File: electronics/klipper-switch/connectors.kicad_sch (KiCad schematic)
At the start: 0 parts

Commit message: schematic naming and pico symbol update
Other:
- title: (none) -> klipper-switch, connectors
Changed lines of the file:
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@@
 	(generator_version "8.0")
 	(paper "A4")
+	(title_block
+		(title "klipper-switch, connectors")
+	)
 )

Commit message: LEDs & Molex CONNs
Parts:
- added D1, D2, D3, D4: 151031SS06000, LED_THT:LED_D3.0mm, symbol klipper-switch:151031SS06000
- added D5, D6, D7: MM3Z18VT1G, Diode_SMD:D_SOD-323_HandSoldering, symbol klipper-switch:MM3Z18VT1G
- added J1, J10, J11, J12, J13, J3, J4, J5, J6, J7, J8, J9: 430450400, KiCAD-RevB-footprint-library:0430450400, symbol klipper-switch:430450400
- added Q1, Q2, Q3: RK7002BMT116, klipper-switch:RK7002BMT116, symbol klipper-switch:RK7002BMT116
- added R1, R2, R3, R4: 100R, Resistor_SMD:R_1206_3216Metric, symbol klipper-switch:RC1206FR-7W100RL
- added R5, R6, R7: 100K, Resistor_SMD:R_1206_3216Metric, symbol klipper-switch:RC1206FR-07100KL
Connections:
- new net: D3.1 (K), Q2.3 (D)
- new net: D3.2 (A), R3.2
- new net: D1.2 (A), R1.2
- new net: D5.1 (K), Q1.2 (G), R5.2
- new net: D4.1 (K), Q3.3 (D)
- new net: D4.2 (A), R4.2
- new net: D2.1 (K), Q1.3 (D)
- new net: D2.2 (A), R2.2
- new net: D7.1 (K), Q3.2 (G), R7.2
- new net: D6.1 (K), Q2.2 (G), R6.2
- new net +12V: J3.2, J3.4, R5.1
- new net +24V: J4.2, J4.4, R6.1
- new net +48V: J5.2, J5.4, R7.1
- new net +5V: J1.2, J1.4, R1.1, R2.1, R3.1, R4.1
- new net GND: D1.1 (K), D5.2 (A), D6.2 (A), D7.2 (A), J1.1, J1.3, J3.1, J3.3, J4.1, J4.3, J5.1, J5.3, Q1.1 (S), Q2.1 (S), Q3.1 (S)
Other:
- note added: "POWER INDICATION LEDs"
- note added: "POWER INPUT CONNECTORs"
- note added: "POWER OUTPIT CONNECTORs"

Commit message: library modified
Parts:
- removed R1, R2, R3, R4: 100R, Resistor_SMD:R_1206_3216Metric, symbol klipper-switch:RC1206FR-7W100RL
- added R1, R2, R3, R4: 100R, Resistor_SMD:R_1206_3216Metric, symbol klipper-switch:RC1206FR-7W100RL_1
- D3: Role LED_12V -> LED_24V
- D4: Role LED_12V -> LED_48V
- J1: Role 05VIN -> 12VIN
- J10, J6: Role 05VIN -> ROLE
- J11, J7: Role 12VIN -> ROLE
- J12, J8: Role 24VIN -> ROLE
- J13, J9: Role 48VIN -> ROLE
- J3: Role 12VIN -> 05VIN
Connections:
- net +12V: now also J1.2, J1.4, R5.2; no longer J3.2, J3.4, R5.1
- net +24V: now also R6.2; no longer R6.1
- net +48V: now also R7.2; no longer R7.1
- net +5V: now also J3.2, J3.4, R1.1, R2.1, R3.1, R4.1; no longer J1.2, J1.4
- net at D3.1 (K): now also R3.2; no longer Q2.3 (D)
- net at D3.2 (A): now also Q2.3 (D)
- net at D1.2 (A): now also R1.2
- net at D5.1 (K), Q1.2 (G): now also R5.1; no longer R5.2
- net at D4.1 (K): now also R4.2; no longer Q3.3 (D)
- net at D4.2 (A): now also Q3.3 (D)
- net at D2.1 (K): now also R2.2; no longer Q1.3 (D)
- net at D2.2 (A): now also Q1.3 (D)
- net at D7.1 (K), Q3.2 (G): now also R7.1; no longer R7.2
- net at D6.1 (K), Q2.2 (G): now also R6.1; no longer R6.2

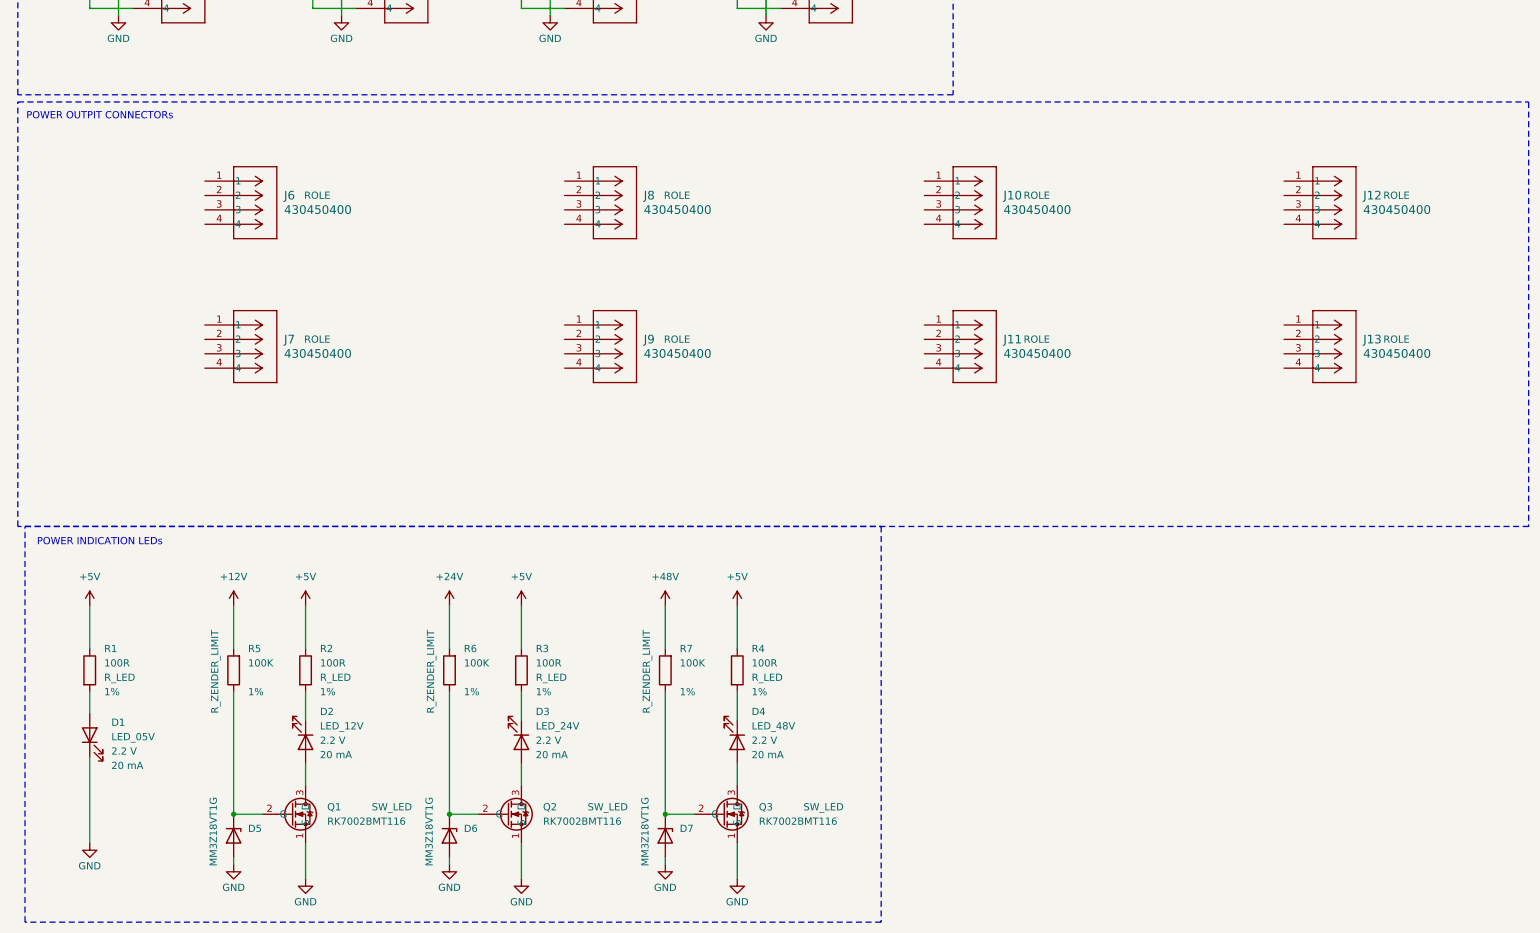
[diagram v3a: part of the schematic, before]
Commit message: output conn adjusted
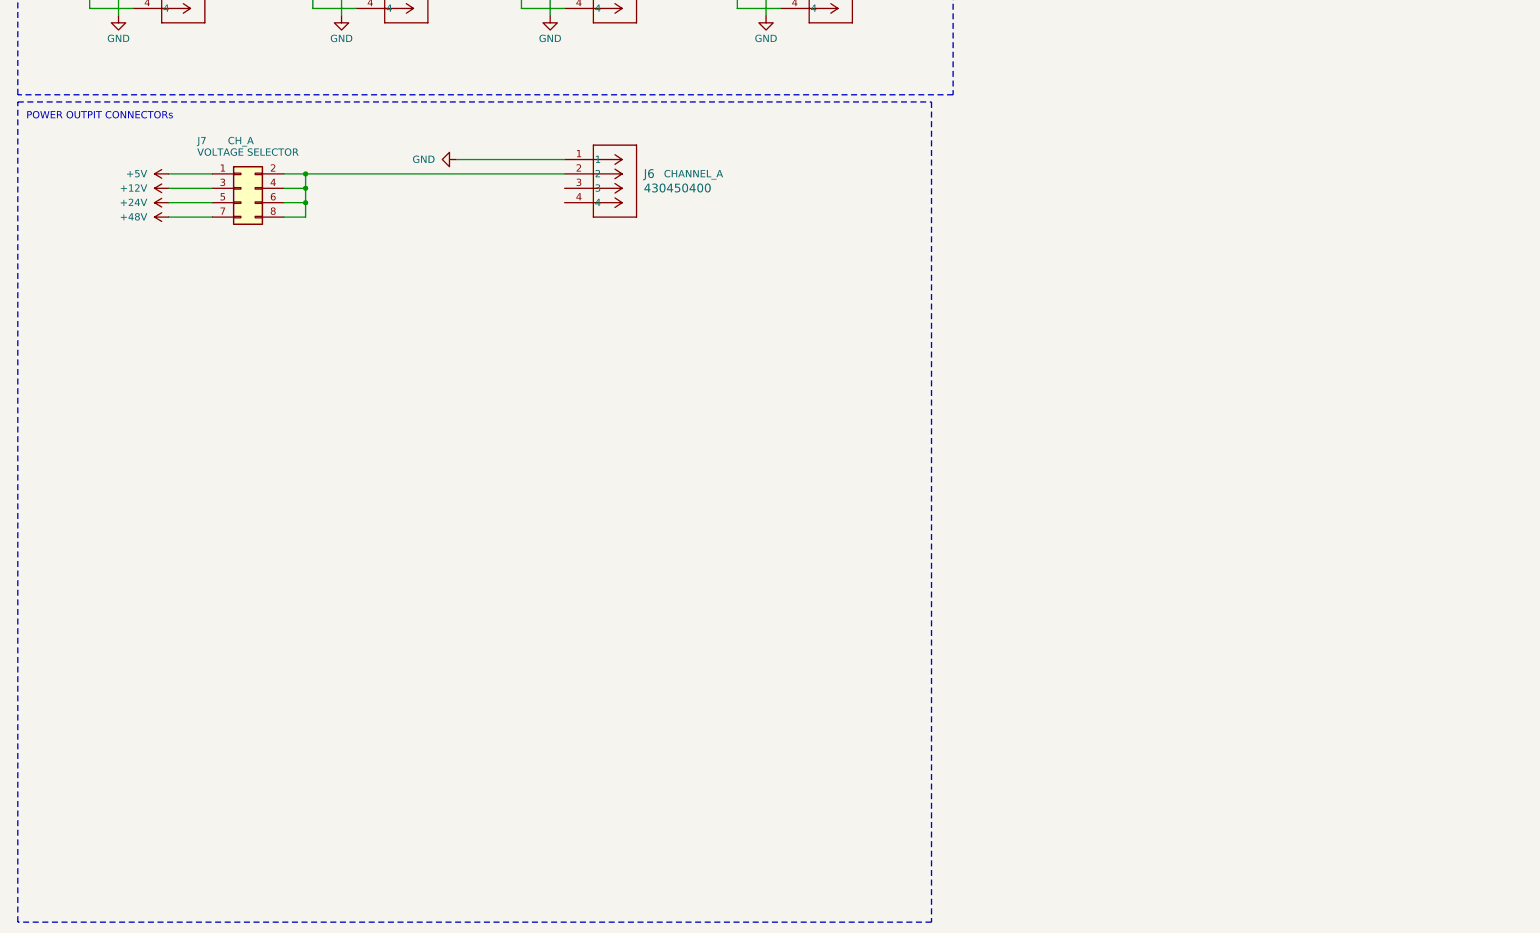
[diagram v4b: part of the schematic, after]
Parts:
- removed D1, D2, D3, D4: 151031SS06000, LED_THT:LED_D3.0mm, symbol klipper-switch:151031SS06000
- removed D5, D6, D7: MM3Z18VT1G, Diode_SMD:D_SOD-323_HandSoldering, symbol klipper-switch:MM3Z18VT1G
- removed J10, J11, J12, J13, J7, J8, J9: 430450400, KiCAD-RevB-footprint-library:0430450400, symbol klipper-switch:430450400
- removed Q1, Q2, Q3: RK7002BMT116, klipper-switch:RK7002BMT116, symbol klipper-switch:RK7002BMT116
- removed R1, R2, R3, R4: 100R, Resistor_SMD:R_1206_3216Metric, symbol klipper-switch:RC1206FR-7W100RL_1
- removed R5, R6, R7: 100K, Resistor_SMD:R_1206_3216Metric, symbol klipper-switch:RC1206FR-07100KL
- added J7: VOLTAGE SELECTOR, Connector_PinHeader_2.54mm:PinHeader_2x04_P2.54mm_Vertical, symbol Connector_Generic:Conn_02x04_Odd_Even
- J6: Role ROLE -> CHANNEL_A
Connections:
- net +12V: now also J7.3 (Pin_3)
- net +24V: now also J7.5 (Pin_5)
- net +48V: now also J7.7 (Pin_7)
- net +5V: now also J7.1 (Pin_1)
- net GND: now also J6.1
- net at J6.2: now also J7.2 (Pin_2), J7.4 (Pin_4), J7.6 (Pin_6), J7.8 (Pin_8)
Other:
- note removed: "POWER INDICATION LEDs"
- moved on the sheet: J6

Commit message: high-side switches added
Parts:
- added J10, J11, J14, J15, J18, J19, J8: VOLTAGE SELECTOR, Connector_PinHeader_2.54mm:PinHeader_2x04_P2.54mm_Vertical, symbol Connector_Generic:Conn_02x04_Odd_Even
- added J12, J13, J16, J17, J20, J21, J9: 430450400, KiCAD-RevB-footprint-library:0430450400, symbol klipper-switch:430450400
- added R10, R12, R13, R16, R17, R20, R21, R9: 5K, Resistor_SMD:R_1206_3216Metric, symbol klipper-switch:RC1206FR-7W100RL_1
- added R11, R14, R15, R18, R19, R22, R23, R8: 1K, Resistor_SMD:R_1206_3216Metric, symbol klipper-switch:RC1206FR-7W100RL_1
- added U2, U3, U4, U5, U6, U7, U8, U9: TPS1HTC30AQPWPRQ1, klipper-switch:TPS1HTC30AQPWPRQ1, symbol klipper-switch:TPS1HTC30AQPWPRQ1
- J6: Role CHANNEL_A -> CH_A
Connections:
- net +12V: now also J10.3 (Pin_3), J11.3 (Pin_3), J14.3 (Pin_3), J15.3 (Pin_3), J18.3 (Pin_3), J19.3 (Pin_3), J8.3 (Pin_3)
- net +24V: now also J10.5 (Pin_5), J11.5 (Pin_5), J14.5 (Pin_5), J15.5 (Pin_5), J18.5 (Pin_5), J19.5 (Pin_5), J8.5 (Pin_5)
- net +48V: now also J10.7 (Pin_7), J11.7 (Pin_7), J14.7 (Pin_7), J15.7 (Pin_7), J18.7 (Pin_7), J19.7 (Pin_7), J8.7 (Pin_7)
- net +5V: now also J10.1 (Pin_1), J11.1 (Pin_1), J14.1 (Pin_1), J15.1 (Pin_1), J18.1 (Pin_1), J19.1 (Pin_1), J8.1 (Pin_1)
- net GND: now also J12.1, J13.1, J16.1, J17.1, J20.1, J21.1, J9.1, R11.2, R14.2, R15.2, R18.2, R19.2, R22.2, R23.2, R8.2, U2.1 (GND), U2.15 (GND), U3.1 (GND), U3.15 (GND), U4.1 (GND), U4.15 (GND), U5.1 (GND), U5.15 (GND), U6.1 (GND), U6.15 (GND), U7.1 (GND), U7.15 (GND), U8.1 (GND), U8.15 (GND), U9.1 (GND), U9.15 (GND)
- net at J6.2, J7.2 (Pin_2), J7.4 (Pin_4)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: now also U2.12 (VS), U2.13 (VS), U2.14 (VS)
- net at J6.3: now also U2.10 (VOUT), U2.8 (VOUT), U2.9 (VOUT)
- net CH_A_DIGITAL_IN: now reaches J6.4
- new net: R17.1, U7.2 (EN)
- new net: J19.2 (Pin_2), J19.4 (Pin_4), J19.6 (Pin_6), J19.8 (Pin_8), J21.2, U9.12 (VS), U9.13 (VS), U9.14 (VS)
- new net: J14.2 (Pin_2), J14.4 (Pin_4), J14.6 (Pin_6), J14.8 (Pin_8), J16.2, U6.12 (VS), U6.13 (VS), U6.14 (VS)
- new net: J16.3, U6.10 (VOUT), U6.8 (VOUT), U6.9 (VOUT)
- new net: R21.1, U9.2 (EN)
- new net: R15.1, U5.6 (SNS)
- new net: R14.1, U4.6 (SNS)
- new net: J9.3, U3.10 (VOUT), U3.8 (VOUT), U3.9 (VOUT)
- new net: J8.2 (Pin_2), J8.4 (Pin_4), J8.6 (Pin_6), J8.8 (Pin_8), J9.2, U3.12 (VS), U3.13 (VS), U3.14 (VS)
- new net: R10.1, U3.2 (EN)
- new net: R11.1, U3.6 (SNS)
- new net: J20.3, U8.10 (VOUT), U8.8 (VOUT), U8.9 (VOUT)
- new net: J18.2 (Pin_2), J18.4 (Pin_4), J18.6 (Pin_6), J18.8 (Pin_8), J20.2, U8.12 (VS), U8.13 (VS), U8.14 (VS)
- new net: R20.1, U8.2 (EN)
- new net: R22.1, U8.6 (SNS)
- new net: R23.1, U9.6 (SNS)
- new net: J13.3, U5.10 (VOUT), U5.8 (VOUT), U5.9 (VOUT)
- new net: J11.2 (Pin_2), J11.4 (Pin_4), J11.6 (Pin_6), J11.8 (Pin_8), J13.2, U5.12 (VS), U5.13 (VS), U5.14 (VS)
- new net: R13.1, U5.2 (EN)
- new net: J15.2 (Pin_2), J15.4 (Pin_4), J15.6 (Pin_6), J15.8 (Pin_8), J17.2, U7.12 (VS), U7.13 (VS), U7.14 (VS)
- new net: J12.3, U4.10 (VOUT), U4.8 (VOUT), U4.9 (VOUT)
- new net: J10.2 (Pin_2), J10.4 (Pin_4), J10.6 (Pin_6), J10.8 (Pin_8), J12.2, U4.12 (VS), U4.13 (VS), U4.14 (VS)
- new net: R12.1, U4.2 (EN)
- new net: R16.1, U6.2 (EN)
- new net: R18.1, U6.6 (SNS)
- new net: J17.3, U7.10 (VOUT), U7.8 (VOUT), U7.9 (VOUT)
- new net: R19.1, U7.6 (SNS)
- new net: J21.3, U9.10 (VOUT), U9.8 (VOUT), U9.9 (VOUT)
- new net: R9.1, U2.2 (EN)
- new net: R8.1, U2.6 (SNS)
- new net CH_A_DIGITAL_OUT: R21.2, R9.2
- new net CH_B_DIGITAL_IN: J12.4
- new net CH_B_DIGITAL_OUT: R12.2
- new net CH_C_DIGITAL_IN: J16.4
- new net CH_C_DIGITAL_OUT: R16.2
- new net CH_D_DIGITAL_IN: J20.4
- new net CH_D_DIGITAL_OUT: R20.2
- new net CH_E_DIGITAL_IN: J9.4
- new net CH_E_DIGITAL_OUT: R10.2
- new net CH_F_DIGITAL_IN: J13.4
- new net CH_F_DIGITAL_OUT: R13.2
- new net CH_G_DIGITAL_IN: J17.4
- new net CH_H_DIGITAL_IN: J21.4
- new net CH_H_DIGITAL_OUT: R17.2
- no-connect marks 0 -> 40
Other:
- note added: "HIGH-SIDE SWITCH 6V-60V 2A-16A 55 mOhm"
- moved on the sheet: J6, J7

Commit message: completed rough schematic
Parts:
- added J22, J24, J26, J28: VOLTAGE SELECTOR, Connector_PinHeader_2.54mm:PinHeader_2x04_P2.54mm_Vertical, symbol Connector_Generic:Conn_02x04_Odd_Even
- added J23, J25, J27, J29: 430450400, KiCAD-RevB-footprint-library:0430450400, symbol klipper-switch:430450400
- added R76, R78, R80, R82: 5K, Resistor_SMD:R_1206_3216Metric, symbol klipper-switch:RC1206FR-7W100RL_1
- added R77, R79, R81, R83: 1K, Resistor_SMD:R_1206_3216Metric, symbol klipper-switch:RC1206FR-7W100RL_1
- added U18, U19, U20, U21: TPS1HTC30AQPWPRQ1, klipper-switch:TPS1HTC30AQPWPRQ1, symbol klipper-switch:TPS1HTC30AQPWPRQ1
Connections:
- net +12V: now also J22.3 (Pin_3), J24.3 (Pin_3), J26.3 (Pin_3), J28.3 (Pin_3)
- net +24V: now also J22.5 (Pin_5), J24.5 (Pin_5), J26.5 (Pin_5), J28.5 (Pin_5)
- net +48V: now also J22.7 (Pin_7), J24.7 (Pin_7), J26.7 (Pin_7), J28.7 (Pin_7)
- net +5V: now also J22.1 (Pin_1), J24.1 (Pin_1), J26.1 (Pin_1), J28.1 (Pin_1)
- net CH_A_DIGITAL_OUT: no longer R21.2
- net CH_H_DIGITAL_OUT: now also R21.2; no longer R17.2
- net GND: now also J23.1, J25.1, J27.1, J29.1, R77.2, R79.2, R81.2, R83.2, U18.1 (GND), U18.15 (GND), U19.1 (GND), U19.15 (GND), U20.1 (GND), U20.15 (GND), U21.1 (GND), U21.15 (GND)
- new net: R80.1, U20.2 (EN)
- new net: R77.1, U18.6 (SNS)
- new net: R76.1, U18.2 (EN)
- new net: R79.1, U19.6 (SNS)
- new net: J24.2 (Pin_2), J24.4 (Pin_4), J24.6 (Pin_6), J24.8 (Pin_8), J25.2, U19.12 (VS), U19.13 (VS), U19.14 (VS)
- new net: J26.2 (Pin_2), J26.4 (Pin_4), J26.6 (Pin_6), J26.8 (Pin_8), J27.2, U20.12 (VS), U20.13 (VS), U20.14 (VS)
- new net: J28.2 (Pin_2), J28.4 (Pin_4), J28.6 (Pin_6), J28.8 (Pin_8), J29.2, U21.12 (VS), U21.13 (VS), U21.14 (VS)
- new net: R82.1, U21.2 (EN)
- new net: J23.3, U18.10 (VOUT), U18.8 (VOUT), U18.9 (VOUT)
- new net: J22.2 (Pin_2), J22.4 (Pin_4), J22.6 (Pin_6), J22.8 (Pin_8), J23.2, U18.12 (VS), U18.13 (VS), U18.14 (VS)
- new net: J29.3, U21.10 (VOUT), U21.8 (VOUT), U21.9 (VOUT)
- new net: R83.1, U21.6 (SNS)
- new net: J25.3, U19.10 (VOUT), U19.8 (VOUT), U19.9 (VOUT)
- new net: R78.1, U19.2 (EN)
- new net: J27.3, U20.10 (VOUT), U20.8 (VOUT), U20.9 (VOUT)
- new net: R81.1, U20.6 (SNS)
- new net CH_G_DIGITAL_OUT: R17.2
- new net CH_I_DIGITAL_IN: J23.4
- new net CH_I_DIGITAL_OUT: R76.2
- new net CH_J_DIGITAL_IN: J25.4
- new net CH_J_DIGITAL_OUT: R78.2
- new net CH_K_DIGITAL_IN: J27.4
- new net CH_K_DIGITAL_OUT: R80.2
- new net CH_L_DIGITAL_IN: J29.4
- new net CH_L_DIGITAL_OUT: R82.2
- no-connect marks 40 -> 60
